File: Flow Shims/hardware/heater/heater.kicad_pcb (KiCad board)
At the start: 4 copper layers, 19 x 112.5 mm, 84 parts, among them J1 Conn_01x03, J2 Nano-Fit, Q1 NVTFS5116PL, Q10 NVTFS5116PL, Q11 NVTFS5116PL, Q12 NVTFS5116PL, Q13 NVTFS5116PL, Q14 NVTFS5116PL, Q15 NVTFS5116PL, Q16 NVTFS5116PL, Q17 NVTFS5116PL, Q18 NVTFS5116PL, Q19 NVTFS5116PL, Q2 NVTFS5116PL, Q20 NVTFS5116PL, Q21 NVTFS5116PL, Q22 NVTFS5116PL, Q23 NVTFS5116PL, Q24 NVTFS5116PL, Q25 NVTFS5116PL, Q3 NVTFS5116PL, Q4 NVTFS5116PL, Q5 NVTFS5116PL, Q6 NVTFS5116PL, Q7 NVTFS5116PL, Q8 NVTFS5116PL, Q9 NVTFS5116PL, U1 ADG5206, U10 TSZ181, U11 TSZ181, U12 TSZ181, U13 TSZ181, U14 TSZ181, U15 TSZ181, U16 TSZ181, U17 TSZ181, U18 TSZ181, U19 TSZ181, U2 ADG5206, U20 TSZ181, U21 TSZ181, U22 TSZ181, U23 TSZ181, U24 TSZ181, U25 TSZ181, U26 TSZ181, U27 TSZ181, U3 TSZ181, U4 TSZ181, U5 TSZ181, U6 TSZ181, U7 TSZ181, U8 TSZ181, U9 TSZ181

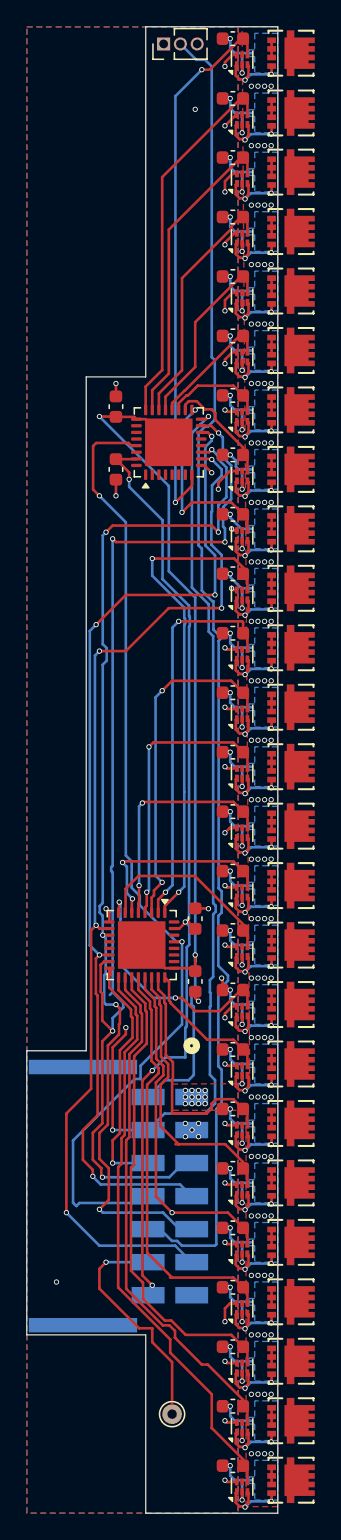
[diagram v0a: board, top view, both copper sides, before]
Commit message: TS25 PCBs fit in CAD
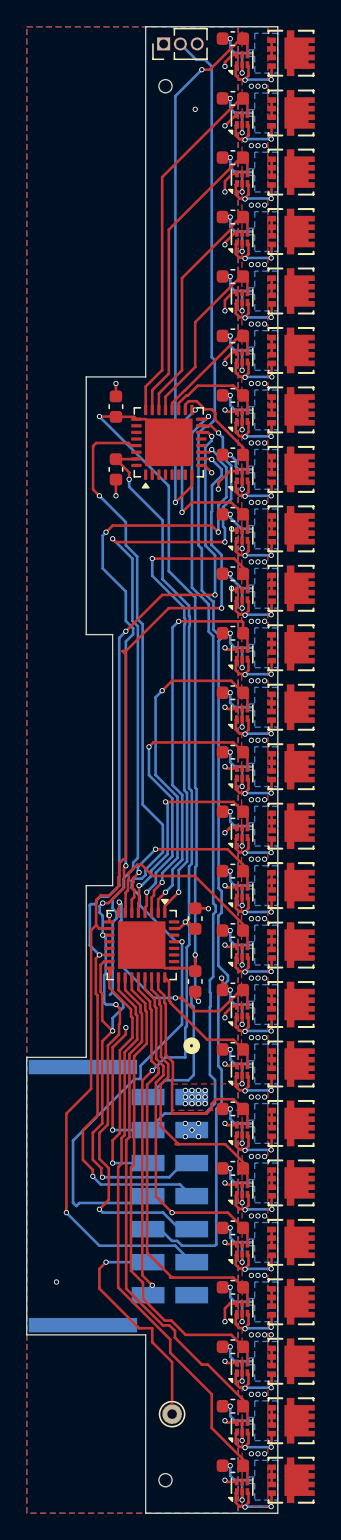
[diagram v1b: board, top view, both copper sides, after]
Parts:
- U10, U11, U12, U13, U14, U15, U16, U17, U18, U19, U20, U21, U22, U23, U24, U25, U26, U27, U3, U4, U5, U6, U7, U8, U9: footprint Package_DFN_QFN:DFN-6_1.3x1.2mm_P0.4mm -> thermalshims:DFN-6_1.3x1.2mm_P0.4mm
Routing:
- net /VG: track 74.1 -> 76.5 mm
- net /A2: track 79.0 -> 80.9 mm, vias 6 -> 8
- net /A0: track 82.8 -> 84.5 mm
- net /VG13: track 21.6 -> 23.1 mm
- net /VG10: track 14.5 -> 15.7 mm
- net /A1: track 75.4 -> 74.3 mm
- net /VG14: track 25.7 -> 26.7 mm
- net /VG12: track 17.8 -> 17.0 mm
- net /VG15: track 29.8 -> 30.4 mm
- net GND: track 136.9 -> 136.3 mm
- net /A3: track 79.4 -> 79.0 mm, vias 5 -> 3
- net VD: vias 108 -> 85
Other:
- outline, holes or cut-outs redrawn
